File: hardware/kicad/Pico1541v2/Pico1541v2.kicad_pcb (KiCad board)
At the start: 2 copper layers, 100 x 76.2 mm, 62 parts, among them J1 SWD, J2 Serial, J3 Display/Keys, J4 Micro SD Card, J5 5V_EXT, J6 USB_A, J7 OLED/Key_Hat, J8 OLED, J9 DIN-6, Q1 MMBT3904, SW1 Reset, SW2 Button1, SW3 Button3, SW4 Button2, SW5 Button4, U1 74LS05, U2 SRV05-4

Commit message: More work on v2 hardware version.
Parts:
- removed the C5 at (150.5, 115.1)
- removed C6: 47u, Capacitor_SMD:CP_Elec_5x5.4
- removed the D1 at (116.6, 67.8)
- removed the J5 at (105.7, 64.2)
- removed the J6 at (150.5, 118.4)
- removed JP1: EXT_5V, Jumper:SolderJumper-2_P1.3mm_Bridged_RoundedPad1.0x1.5mm
- removed REF** (x4): Symbol_CreativeCommons_SilkScreenTop_Type2_Big, Symbol:Symbol_CreativeCommons_SilkScreenTop_Type2_Big
- removed REF** (x4): Symbol_CC-Noncommercial_CopperTop_Small, Symbol:Symbol_CC-Noncommercial_CopperTop_Small
- removed REF**: KiCad-Logo2_12mm_SilkScreen, Symbol:KiCad-Logo2_12mm_SilkScreen
- added R4: 1k, Resistor_SMD:R_0603_1608Metric_Pad0.98x0.95mm_HandSolder, F.Cu at (177.6, 67.3)
- C1: footprint Capacitor_SMD:CP_Elec_5x5.4 -> Capacitor_SMD:CP_Elec_5x4.5
- C3: value 47u -> 10u; footprint Capacitor_SMD:CP_Elec_5x5.4 -> Capacitor_SMD:C_0603_1608Metric_Pad1.08x0.95mm_HandSolder
- D1: renamed from D2; footprint Pico1541-footprints:LED_D5.0mm-4_RGB_CorrectStaggered_Pins -> Pico1541 Footprints:LED_D5.0mm-4_RGB_CorrectStaggered_Pins
- J4: footprint Pico1541-footprints:MicroSD_HPJF -> Pico1541 Footprints:MicroSD_HPJF
- J7: renamed from J9; footprint Pico1541-footprints:DIN-6-240deg -> Pico1541 Footprints:DIN-6-240deg
- RN3, RN4: value 4k7 -> 1k
- SW3: value Button3 -> Button2
- SW4: renamed from SW5; value Button4 -> Button3
- SW5: renamed from SW4; value Button2 -> Button4
- moved C1 64.7 mm to (179.9, 60.1)
- moved C3 58.9 mm to (151.9, 111.0), turned to 0 degrees
- moved RN1 19.4 mm to (140.1, 118.0)
- moved J4 18.2 mm to (152.2, 124.7)
- moved C2 18.1 mm to (151.1, 113.8)
- moved R3 16.8 mm to (140.1, 113.8)
- moved D2 15.8 mm to (136.1, 125.8)
- moved D1 15.8 mm to (128.7, 126.6)
- moved SW5 6.55 mm to (194.3, 85.0)
- moved SW4 6.55 mm to (187.8, 85.0)
- renumbered C7 to C5, D3 to D2, J7 to J5, J8 to J6, R2 to R1, R1 to R2
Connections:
- A1 pad 39: VS -> unconnected-(A1-VSYS-Pad39)
- A1 pad 40: VBUS -> +5V
- A1 pad TP1: GND -> unconnected-(A1-USB_GND-PadTP1)
- A1 pad TP2: /USB_DN -> unconnected-(A1-USB_DM-PadTP2)
- A1 pad TP3: /USB_DP -> unconnected-(A1-USB_DP-PadTP3)
- C1 pad 1: +3.3V -> +5V
- C3 pad 1: +5V -> +3.3V
- J5 pad 5: Net-(J7-Pin_5) -> Net-(J5-Pin_5)
- J5 pad 6: Net-(J7-Pin_6) -> Net-(J5-Pin_6)
- J5 pad 7: Net-(J7-Pin_7) -> Net-(J5-Pin_7)
- J5 pad 8: Net-(J7-Pin_8) -> Net-(J5-Pin_8)
- SW2 pad 1: Net-(J7-Pin_8) -> Net-(J5-Pin_5)
- SW2 pad 2: Net-(J7-Pin_6) -> GNDA
- SW3 pad 1: Net-(J7-Pin_8) -> Net-(J5-Pin_6)
- SW3 pad 2: Net-(J7-Pin_5) -> GNDA
- SW4 pad 1: Net-(J7-Pin_7) -> Net-(J5-Pin_7)
- SW4 pad 2: Net-(J7-Pin_5) -> GNDA
- SW5 pad 1: Net-(J7-Pin_7) -> Net-(J5-Pin_8)
- SW5 pad 2: Net-(J7-Pin_6) -> GNDA
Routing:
- net +3.3V: track 134.9 -> 48.9 mm, vias 5 -> 2
- net /PLED_N: track 79.2 -> 0.00 mm
- net /USB_DN: track 73.3 -> 0.00 mm, vias 1 -> 0
- net /USB_DP: track 73.3 -> 0.00 mm, vias 1 -> 0
- net Net-(J7-Pin_8): track 71.2 -> 0.00 mm, vias 1 -> 0
- net Net-(J7-Pin_6): track 63.9 -> 0.00 mm, vias 2 -> 0
- net Net-(J7-Pin_5): track 63.7 -> 0.00 mm, vias 1 -> 0
- net Net-(J7-Pin_7): track 57.5 -> 0.00 mm, vias 2 -> 0
- net Net-(J5-Pin_5): track 0.00 -> 50.9 mm, vias 0 -> 1
- net Net-(J5-Pin_6): track 0.00 -> 49.5 mm, vias 0 -> 1
- net /SD_CD: track 48.2 -> 0.00 mm
- net Net-(J5-Pin_7): track 0.00 -> 47.9 mm, vias 0 -> 1
- net Net-(J5-Pin_8): track 0.00 -> 45.8 mm, vias 0 -> 1
- net /SD_DAT0: track 41.5 -> 0.00 mm
- net /SD_CMD: track 38.0 -> 0.00 mm
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
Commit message: Re-instanciated the RAM_POINTER for dumping ram.
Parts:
- moved H6 36.7 mm to (182.3, 42.5)
- moved H1 36.5 mm to (78.3, 43.0)
- moved J1 32.2 mm to (132.2, 108.8), turned to -90 degrees
- moved C1 31.8 mm to (151.8, 74.9)
- moved H2 22.6 mm to (80.1, 123.0)
- moved J2 19.3 mm to (114.2, 63.8)
- moved RN2 16.8 mm to (129.8, 118.8)
- moved H3 16.6 mm to (174.1, 139.3)
- moved FID6 11.0 mm to (91.0, 124.7)
- moved FID5 9.35 mm to (92.2, 118.6)
- moved U2 3.25 mm to (158.7, 74.5)
- moved J7 0.18 mm to (156.9, 64.5)
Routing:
- net +5V: track 141.0 -> 17.8 mm, vias 3 -> 2
- net Net-(A1-RUN): track 59.1 -> 0.00 mm, vias 1 -> 0
- net Net-(A1-GPIO28_ADC2): track 44.9 -> 0.00 mm, vias 2 -> 0
- net Net-(A1-SWDIO): track 41.7 -> 0.00 mm, vias 2 -> 0
- net Net-(A1-SWCLK): track 41.5 -> 0.00 mm, vias 2 -> 0
- net Net-(A1-GPIO27_ADC1): track 40.9 -> 0.00 mm, vias 2 -> 0
- net Net-(A1-GPIO1): track 39.2 -> 0.00 mm, vias 1 -> 0
- net Net-(A1-GPIO0): track 37.8 -> 0.00 mm, vias 1 -> 0
- net Net-(A1-GPIO26_ADC0): track 37.6 -> 0.00 mm, vias 2 -> 0
- net /DATA_IEC: track 47.8 -> 12.2 mm
- net Net-(A1-GPIO22): track 33.2 -> 0.00 mm, vias 2 -> 0
- net unconnected-(A1-VSYS-Pad39): track 30.9 -> 1.19 mm, vias 2 -> 0
- net /CLK_IEC: track 41.5 -> 12.3 mm
- net /ATN_IEC: track 45.9 -> 17.2 mm
- net /RESET_IEC: track 32.3 -> 5.69 mm, vias 2 -> 0
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
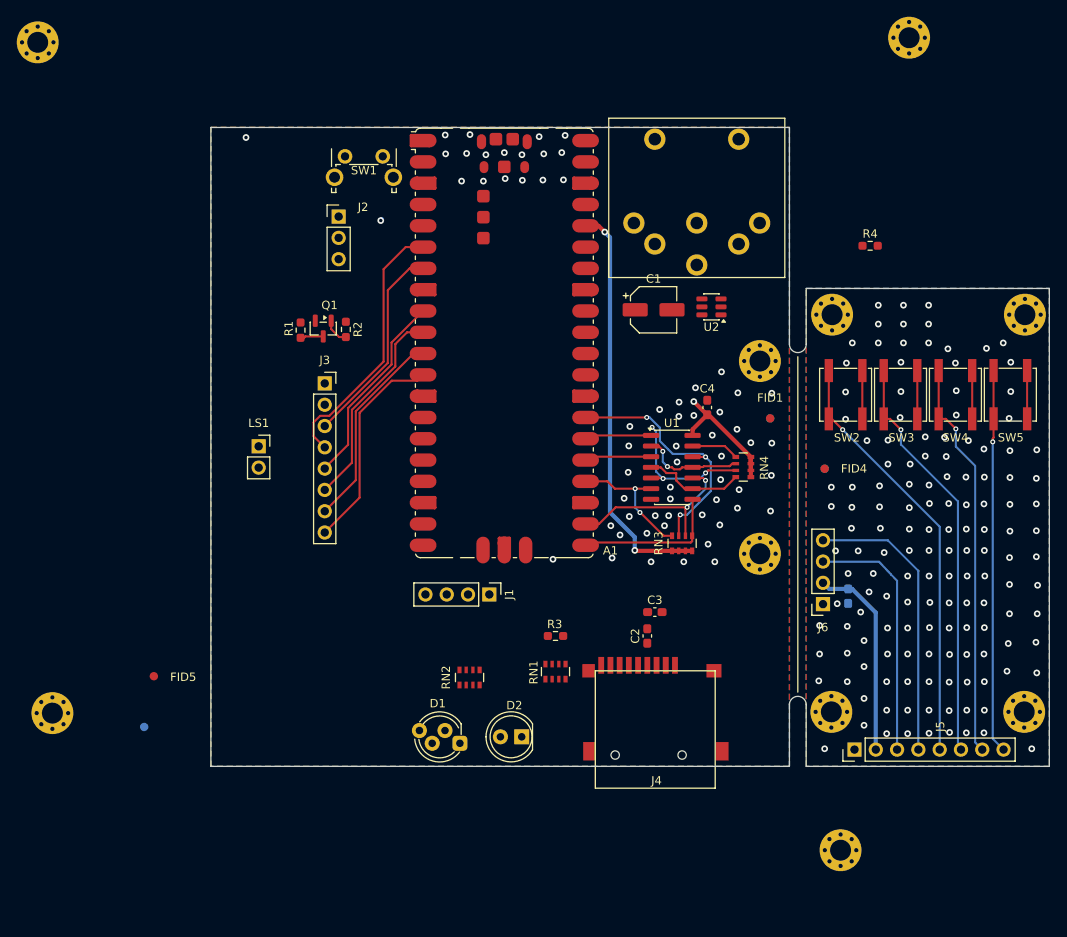
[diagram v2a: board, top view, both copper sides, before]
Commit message: Use real-time sampling of ATN signal if the IRQ flag is false. Not fixing the real issue, but seems to not impact performance any significantly.
More updates on the hardware.
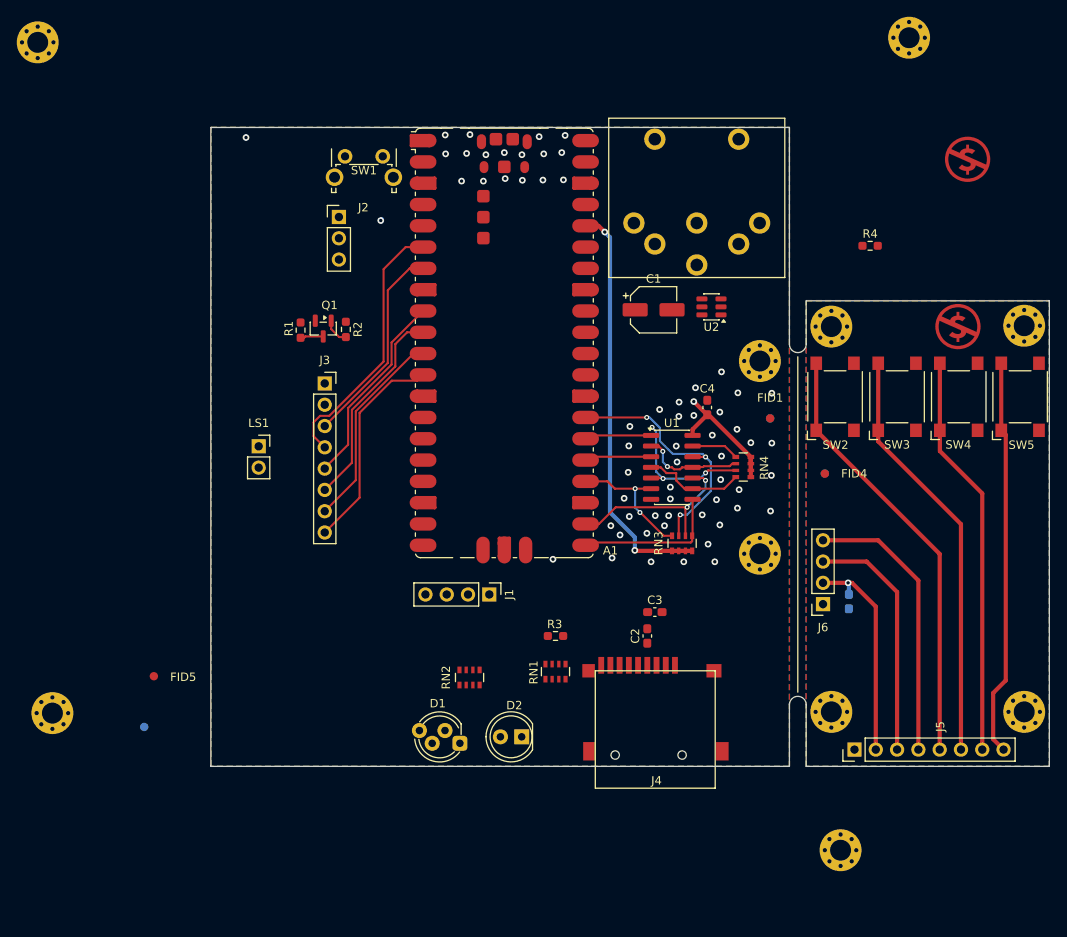
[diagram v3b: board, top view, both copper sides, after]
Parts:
- added LOGO1: ~, Symbol:Symbol_CC-Noncommercial_CopperTop_Small, F.Cu at (189.2, 57.0)
- added LOGO2: ~, Symbol:Symbol_CC-Noncommercial_CopperTop_Small, F.Cu at (188.1, 76.9)
- SW2, SW3, SW4, SW5: footprint Button_Switch_SMD:SW_SPST_EVPBF -> Button_Switch_SMD:SW_SPST_Omron_B3FS-100xP
- U1: value 74LS05 -> 74LS06
- moved H10 23.1 mm to (173.0, 76.9)
- moved H9 22.9 mm to (196.0, 76.8)
- moved SW2 1.28 mm to (173.4, 85.3)
- moved SW5 1.19 mm to (195.5, 85.3)
- moved C5 0.65 mm to (175.1, 109.7)
- moved FID4 0.59 mm to (172.2, 94.4)
- moved FID3 0.57 mm to (172.2, 94.4)
- moved SW3 0.48 mm to (180.8, 85.3)
- moved SW4 0.46 mm to (188.2, 85.3)
- moved J2 0.06 mm to (114.3, 63.8)
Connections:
- A1 pad 21: /DATA_RX -> /SLED_R
- A1 pad 22: /CLK_RX -> /SLED_G
- A1 pad 24: /ATN_RX -> /SLED_B
- A1 pad 25: /DATA_TX -> /DATA_RX
- A1 pad 26: /CLK_TX -> /DATA_TX
- A1 pad 27: /RESET_RX -> /CLK_RX
- A1 pad 29: Net-(A1-GPIO22) -> /CLK_TX
- A1 pad 31: Net-(A1-GPIO26_ADC0) -> /ATN_RX
- A1 pad 32: Net-(A1-GPIO27_ADC1) -> /RESET_RX
- A1 pad 34: Net-(A1-GPIO28_ADC2) -> /ALED_P
- A1 pad 5: /PLED_N -> /ALED_N
- RN2 pad 1: Net-(A1-GPIO22) -> /ALED_P
- RN2 pad 2: Net-(A1-GPIO26_ADC0) -> /SLED_R
- RN2 pad 3: Net-(A1-GPIO27_ADC1) -> /SLED_G
- RN2 pad 4: Net-(A1-GPIO28_ADC2) -> /SLED_B
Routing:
- net GNDA: track 23.2 -> 0.00 mm, vias 142 -> 0
- net +3.3VA: track 24.1 -> 25.9 mm, vias 0 -> 1
- net Net-(J5-Pin_8): track 45.8 -> 47.4 mm, vias 1 -> 0
- net Net-(J5-Pin_5): track 50.9 -> 52.2 mm, vias 1 -> 0
- net Net-(J5-Pin_3): track 30.0 -> 29.1 mm
- net Net-(J5-Pin_6): track 49.5 -> 50.2 mm, vias 1 -> 0
- net Net-(J5-Pin_4): track 34.2 -> 33.5 mm
- net Net-(J5-Pin_7): track 47.9 -> 48.2 mm, vias 1 -> 0
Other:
- outline, holes or cut-outs redrawn

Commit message: Updated V2 hardware.
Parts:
- moved R1 37.5 mm to (117.6, 114.0), turned to 0 degrees
- moved Q1 34.5 mm to (117.4, 111.3), turned to 0 degrees
- moved R2 31.5 mm to (117.5, 108.6), turned to 0 degrees
- moved LS1 26.5 mm to (78.5, 95.0)
- moved RN1 24.2 mm to (163.9, 122.2), turned to 180 degrees
- moved J3 3.27 mm to (114.4, 80.9)
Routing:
- net +3.3V: track 48.9 -> 0.00 mm, vias 2 -> 0
- net Net-(A1-GPIO4): track 31.7 -> 0.00 mm
- net /RESET_RX: track 30.5 -> 0.00 mm, vias 3 -> 0
- net /KEY4: track 25.4 -> 0.00 mm
- net /KEY2: track 24.8 -> 0.00 mm
- net Net-(A1-GPIO5): track 24.6 -> 0.00 mm
- net /KEY3: track 24.3 -> 0.00 mm
- net /KEY1: track 23.7 -> 0.00 mm
- net /CLK_RX: track 22.2 -> 0.00 mm, vias 2 -> 0
- net /DATA_RX: track 17.9 -> 0.00 mm
- net +5V: track 17.8 -> 0.00 mm, vias 2 -> 0
- net /ATN_IEC: track 17.2 -> 0.00 mm, vias 3 -> 0
- net /ATN_RX: track 16.2 -> 0.00 mm, vias 2 -> 0
- net /CLK_IEC: track 12.3 -> 0.00 mm, vias 2 -> 0
- net /DATA_IEC: track 12.2 -> 0.00 mm
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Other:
- board size 100 x 76.2 mm -> 86.8 x 76.2 mm

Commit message: More hardware updates.
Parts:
- moved FID1 52.8 mm to (114.5, 74.9)
- moved FID2 52.8 mm to (114.5, 74.9)
- moved C2 32.5 mm to (150.2, 146.3)
- moved C3 32.5 mm to (151.1, 143.5)
- moved R3 32.5 mm to (139.2, 146.3)
- moved R4 28.7 mm to (160.2, 44.5)
- moved H3 24.0 mm to (165.0, 117.1)
- moved Q1 20.4 mm to (99.0, 102.5)
- moved R1 20.4 mm to (99.2, 105.2)
- moved R2 20.4 mm to (99.1, 99.8)
- moved J1 17.9 mm to (114.4, 108.7), turned to 0 degrees
- moved RN1 12.2 mm to (161.0, 110.4)
- moved D2 12.0 mm to (131.4, 114.8)
- moved D1 12.0 mm to (124.0, 115.5)
- moved RN2 9.77 mm to (131.5, 109.1)
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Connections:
- A1 pad 14: unconnected-(A1-GPIO10-Pad14) -> /ALED_P
- A1 pad 34: /ALED_P -> unconnected-(A1-GPIO28_ADC2-Pad34)
- D2 pad 2: /PLED_N -> /ALED_N
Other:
- board size 86.8 x 76.2 mm -> 86.9 x 66.9 mm

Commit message: More hardware updates.
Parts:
- removed H6: M, MountingHole:MountingHole_2.5mm_Pad_Via
- moved FID6 76.6 mm to (136.0, 62.6)
- moved FID1 58.5 mm to (165.5, 103.7), turned to 180 degrees
- moved FID2 58.5 mm to (165.5, 103.7), turned to 0 degrees
- moved H1 45.2 mm to (118.8, 63.4)
- moved FID5 44.7 mm to (136.9, 117.7), turned to 90 degrees
- moved R4 40.6 mm to (152.0, 84.3), turned to 180 degrees
- moved Q1 38.6 mm to (97.2, 63.9)
- moved R1 38.6 mm to (97.4, 66.6)
- moved R2 38.6 mm to (97.3, 61.2)
- moved H2 35.6 mm to (115.2, 117.1)
- moved RN2 9.00 mm to (122.5, 108.4)
- moved LOGO2 7.64 mm to (180.5, 67.8), turned to -90 degrees
- moved J1 4.32 mm to (114.0, 104.4)
- moved RN3 4.09 mm to (153.8, 98.9)
- moved J3 2.54 mm to (114.2, 78.4)
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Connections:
- RN3 pad 6: /CLK_RX -> /RESET_RX
- RN3 pad 7: /RESET_RX -> /ATN_RX
- RN3 pad 8: /ATN_RX -> /CLK_RX
- RN4 pad 6: /CLK_IEC -> /ATN_IEC
- RN4 pad 7: /ATN_IEC -> /CLK_IEC
- U1 pad 1: /CLK_TX -> /ATN_IEC
- U1 pad 10: /CLK_RX -> /CLK_IEC
- U1 pad 11: /CLK_IEC -> /CLK_TX
- U1 pad 2: /CLK_IEC -> /ATN_RX
- U1 pad 3: /DATA_TX -> /CLK_IEC
- U1 pad 4: /DATA_IEC -> /CLK_RX
- U1 pad 5: /ATN_IEC -> /DATA_TX
- U1 pad 6: /ATN_RX -> /DATA_IEC
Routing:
- net +3.3V: track 0.00 -> 49.2 mm, vias 0 -> 2
- net +5V: track 0.00 -> 48.2 mm
- net /CLK_IEC: track 0.00 -> 41.7 mm, vias 0 -> 2
- net /DATA_IEC: track 0.00 -> 41.4 mm, vias 0 -> 2
- net /ATN_IEC: track 0.00 -> 38.3 mm, vias 0 -> 2
- net Net-(A1-RUN): track 0.00 -> 37.9 mm, vias 0 -> 1
- net /SD_DAT0: track 0.00 -> 34.7 mm
- net /SD_CD: track 0.00 -> 34.6 mm
- net /RESET_RX: track 0.00 -> 33.4 mm, vias 0 -> 2
- net /SD_CMD: track 0.00 -> 32.4 mm
- net /SD_CLK: track 0.00 -> 29.5 mm
- net /ATN_RX: track 0.00 -> 27.9 mm, vias 0 -> 2
- net /RESET_IEC: track 0.00 -> 25.1 mm, vias 0 -> 2
- net /CLK_RX: track 0.00 -> 17.7 mm, vias 0 -> 2
- net /DATA_RX: track 0.00 -> 17.1 mm
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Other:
- board size 86.9 x 66.9 mm -> 86.4 x 66.9 mm

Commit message: More hardware v2 updates
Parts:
- removed LOGO1, LOGO2: ~, Symbol:Symbol_CC-Noncommercial_CopperTop_Small
- removed R3: 10K, Resistor_SMD:R_0603_1608Metric_Pad0.98x0.95mm_HandSolder
- added CC1: ~, Symbol:Symbol_CC-Noncommercial_CopperTop_Small, F.Cu at (180.6, 67.8)
- added CC2: ~, Symbol:Symbol_CC-Noncommercial_CopperTop_Small, F.Cu at (164.4, 110.6)
- added REF**: Symbol_CreativeCommons_SilkScreenTop_Type2_Big, Symbol:Symbol_CreativeCommons_SilkScreenTop_Type2_Big, F.Cu at (191.9, 88.9)
- added REF**: Symbol_CreativeCommons_SilkScreenTop_Type2_Big, Symbol:Symbol_CreativeCommons_SilkScreenTop_Type2_Big, F.Cu at (134.3, 80.9)
- added REF**: Mousebites_1.0mm, Pico1541-footprints:Mousebites_1.5mm, F.Cu at (168.8, 87.1)
- added REF**: Mousebites_1.0mm, Pico1541-footprints:Mousebites_1.5mm, F.Cu at (168.8, 95.9)
- added REF**: Symbol_CreativeCommons_SilkScreenTop_Type2_Big, Symbol:Symbol_CreativeCommons_SilkScreenTop_Type2_Big, B.Cu at (158.5, 109.2)
- added REF**: KiCad-Logo2_12mm_SilkScreen, Symbol:KiCad-Logo2_12mm_SilkScreen, B.Cu at (140.0, 94.2)
- added REF**: Symbol_CreativeCommons_SilkScreenTop_Type2_Big, Symbol:Symbol_CreativeCommons_SilkScreenTop_Type2_Big, B.Cu at (191.9, 89.0)
- D1: footprint Pico1541 Footprints:LED_D5.0mm-4_RGB_CorrectStaggered_Pins -> Pico1541-footprints:LED_D5.0mm-4_RGB_CorrectStaggered_Pins
- D2: value PWR_STATE -> LED_ACT
- J4: footprint Pico1541 Footprints:MicroSD_HPJF -> Pico1541-footprints:MicroSD_HPJF
- J7: footprint Pico1541 Footprints:DIN-6-240deg -> Pico1541-footprints:DIN-6-240deg
- moved LS1 49.7 mm to (120.3, 68.0), turned to -90 degrees
- moved C2 40.3 mm to (147.6, 106.1), turned to 180 degrees
- moved C3 37.7 mm to (155.5, 106.1)
- moved R2 22.4 mm to (117.6, 70.7), turned to 180 degrees
- moved Q1 22.2 mm to (117.3, 73.2)
- moved R1 22.1 mm to (117.5, 75.7), turned to 180 degrees
- moved FID5 19.5 mm to (119.2, 109.4)
- moved RN2 16.4 mm to (136.5, 117.0), turned to 180 degrees
- moved RN1 10.3 mm to (153.7, 103.0), turned to 0 degrees
- moved D1 0.21 mm to (124.2, 115.6)
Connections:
- net /SD_DET renamed /DET_SD
- RN1 pad 1: +3.3V -> /SD_DAT0
- RN1 pad 2: +3.3V -> /SD_CLK
- RN1 pad 3: +3.3V -> /SD_CMD
- RN1 pad 4: +3.3V -> /SD_CD
- RN1 pad 5: /SD_CD -> +3.3V
- RN1 pad 6: /SD_CMD -> +3.3V
- RN1 pad 7: /SD_CLK -> +3.3V
- RN1 pad 8: /SD_DAT0 -> +3.3V
- RN2 pad 1: /ALED_P -> /SLED_B
- RN2 pad 2: /SLED_R -> /SLED_G
- RN2 pad 3: /SLED_G -> /SLED_R
- RN2 pad 4: /SLED_B -> /ALED_P
- RN2 pad 5: Net-(D1-BA) -> Net-(D2-KA)
- RN2 pad 6: Net-(D1-GA) -> Net-(D1-RA)
- RN2 pad 7: Net-(D1-RA) -> Net-(D1-GA)
- RN2 pad 8: Net-(D2-KA) -> Net-(D1-BA)
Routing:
- net +3.3V: track 49.2 -> 118.4 mm, vias 2 -> 4
- net /ALED_N: track 0.00 -> 62.0 mm
- net /SLED_B: track 0.00 -> 53.7 mm, vias 0 -> 2
- net /SLED_G: track 0.00 -> 51.5 mm, vias 0 -> 2
- net /SLED_R: track 0.00 -> 50.2 mm, vias 0 -> 2
- net +5V: track 48.2 -> 91.4 mm, vias 0 -> 2
- net /ALED_P: track 0.00 -> 42.7 mm
- net /DET_SD: track 0.00 -> 36.7 mm, vias 0 -> 2
- net Net-(A1-GPIO4): track 0.00 -> 30.1 mm
- net Net-(A1-SWDIO): track 0.00 -> 28.1 mm, vias 0 -> 1
- net Net-(A1-SWCLK): track 0.00 -> 25.7 mm, vias 0 -> 1
- net Net-(A1-GPIO5): track 0.00 -> 21.0 mm
- net /KEY2: track 0.00 -> 19.5 mm
- net Net-(D1-BA): track 0.00 -> 19.2 mm
- net /KEY4: track 0.00 -> 19.1 mm
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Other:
- outline, holes or cut-outs redrawn
- board text added: "Pico1541 - v2"
- board text removed: "Pico1541 - v1"

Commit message: Added 1K pull-up on the data output pin, to make it possible to drive high by configuring the pin as an input. This can be done independently of the pin state, resulting in a hardware ATN ack function that is both simple and bullet proof.
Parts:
- removed the REF** at (168.8, 87.1)
- removed the REF** at (168.8, 95.9)
- added R3: 1k, Resistor_SMD:R_0603_1608Metric_Pad0.98x0.95mm_HandSolder, F.Cu at (148.0, 92.8)
- D1: footprint Pico1541-footprints:LED_D5.0mm-4_RGB_CorrectStaggered_Pins -> Pico-1541 Footprints:LED_D5.0mm-4_RGB_CorrectStaggered_Pins
- J4: footprint Pico1541-footprints:MicroSD_HPJF -> Pico-1541 Footprints:MicroSD_HPJF
- J7: footprint Pico1541-footprints:DIN-6-240deg -> Pico-1541 Footprints:DIN-6-240deg
- moved REF** 29.5 mm to (136.0, 110.4)
- moved C3 1.27 mm to (154.3, 105.9)
- moved C2 0.20 mm to (147.6, 105.9)
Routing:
- net +3.3V: track 118.4 -> 120.2 mm
- net /SD_CLK: track 44.3 -> 42.9 mm
- net /DATA_TX: track 8.19 -> 8.80 mm
- net GND: track 4.57 -> 4.99 mm, vias 251 -> 254
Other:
- outline, holes or cut-outs redrawn
